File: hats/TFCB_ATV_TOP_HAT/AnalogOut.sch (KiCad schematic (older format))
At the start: 36 parts

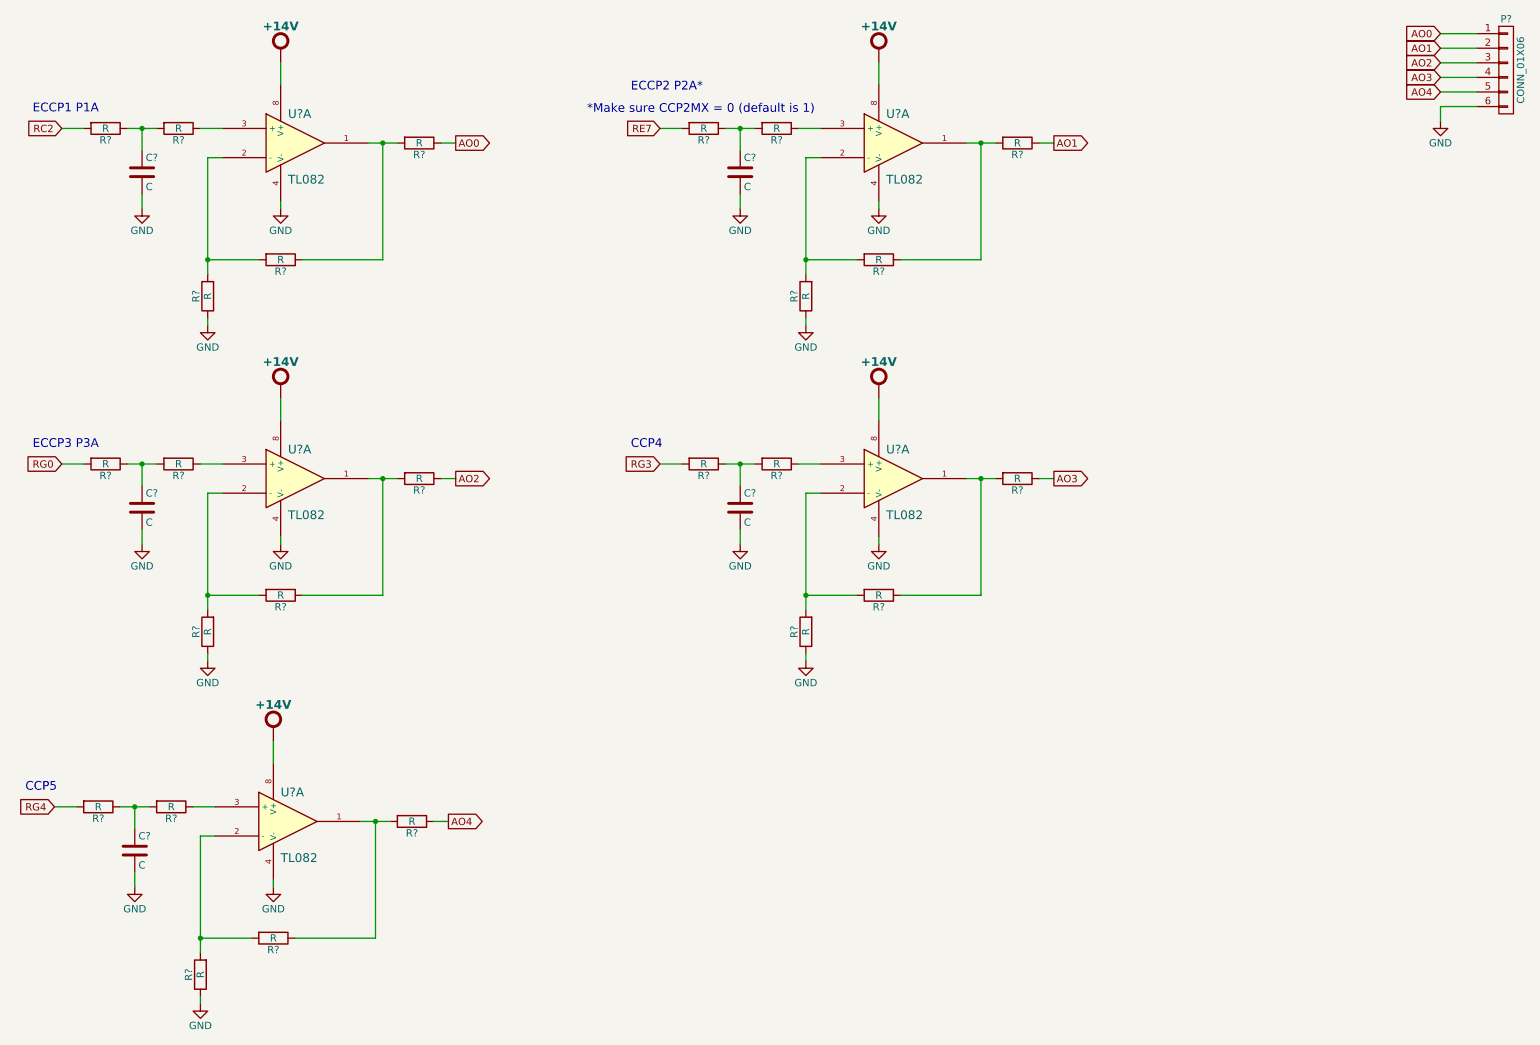
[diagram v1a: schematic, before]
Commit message: Added scanner trigger and current sense cct
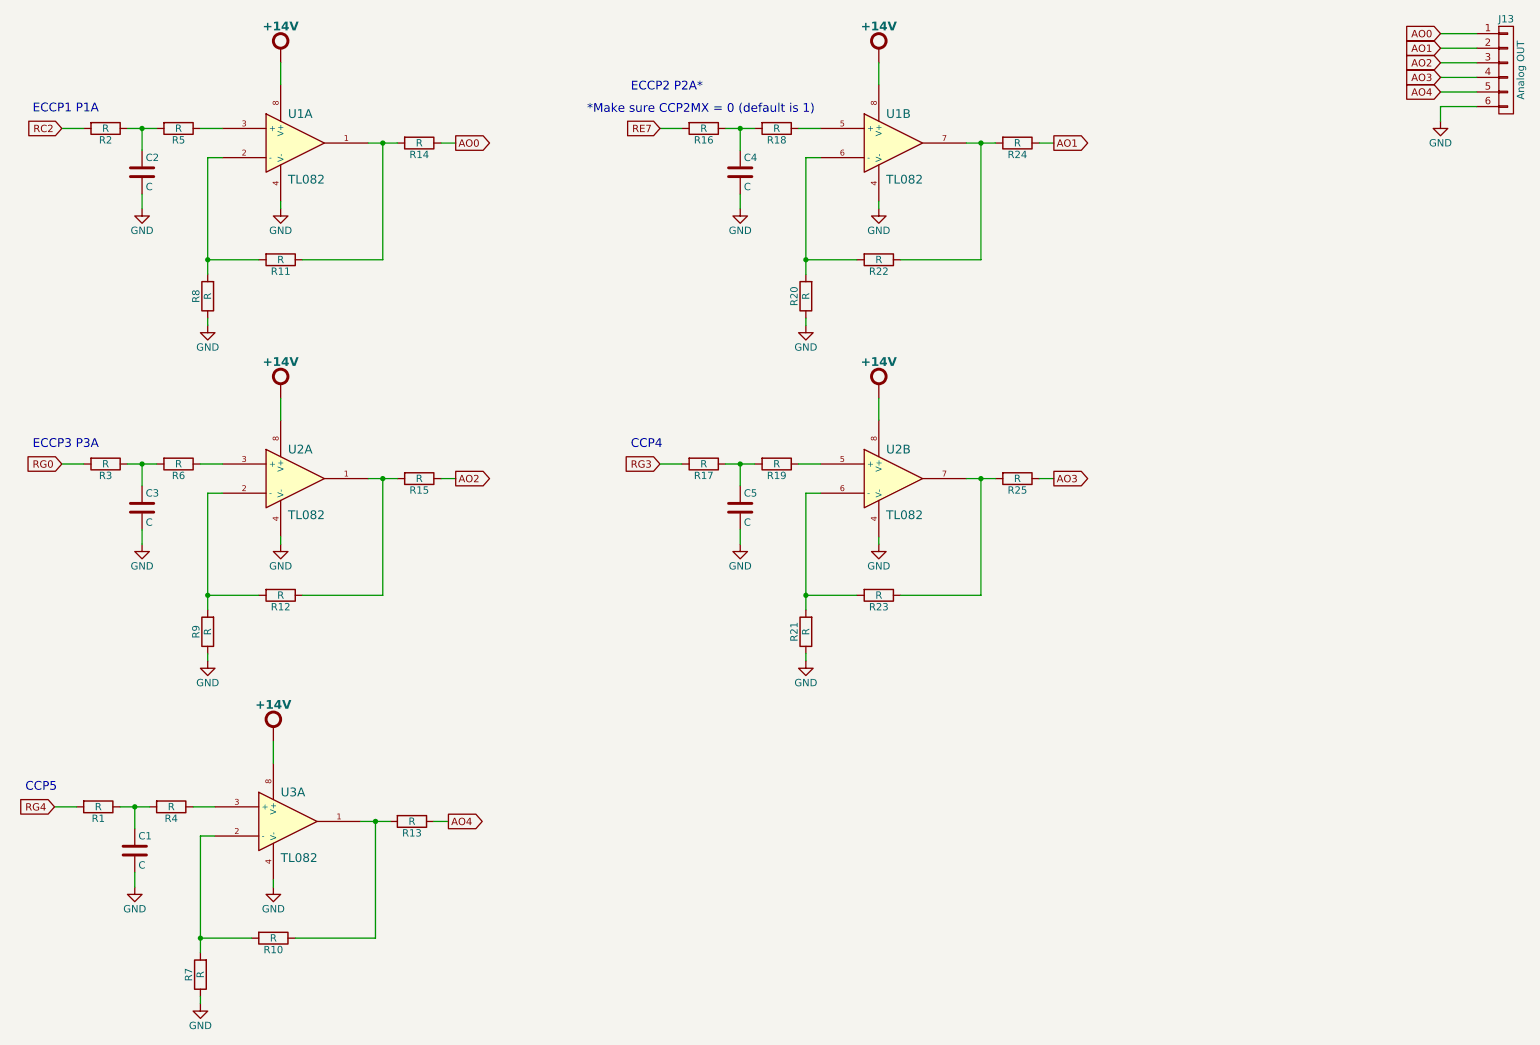
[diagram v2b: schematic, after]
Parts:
- C1, C2, C3, C4, C5: renamed from C?; footprint (none) -> Capacitors_SMD:C_0805_HandSoldering
- J13: renamed from P?; value CONN_01X06 -> Analog OUT; footprint (none) -> bjh-kicad-connector-fp:Weidmuller-SL-5.08-Vertical-6Pole
- R1, R10, R11, R12, R13, R14, R15, R16, R17, R18, R19, R2, R20, R21, R22, R23, R24, R25, R3, R4, R5, R6, R7, R8, R9: renamed from R?; footprint (none) -> Resistors_SMD:R_0805_HandSoldering
- gave numbers to parts that had none: 3
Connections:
- net at R22.1, R24.2: now also U1.7; no longer U1.1
- net at R20.2, R22.2: now also U1.6 (-); no longer U1.2 (-)
- net at R18.1: now also U1.5 (+); no longer U1.3 (+)
- net at R23.1, R25.2: now also U2.7; no longer U2.1
- net at R21.2, R23.2: now also U2.6 (-); no longer U2.2 (-)
- net at R19.1: now also U2.5 (+); no longer U2.3 (+)

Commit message: latest updates
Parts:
- U1, U2, U3: footprint (none) -> Housings_SOIC:SOIC-8_3.9x4.9mm_Pitch1.27mm
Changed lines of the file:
@@
 F 0 "U1" H 2500 1800 60  0000 L CNN
 F 1 "TL082" H 2500 1350 60  0000 L CNN
-F 2 "" H 2550 1600 60  0001 C CNN
+F 2 "Housings_SOIC:SOIC-8_3.9x4.9mm_Pitch1.27mm" H 2550 1600 60  0001 C CNN
 F 3 "" H 2550 1600 60  0000 C CNN
 	1    2550 1600
@@
 F 0 "U2" H 2500 4100 60  0000 L CNN
 F 1 "TL082" H 2500 3650 60  0000 L CNN
-F 2 "" H 2550 3900 60  0001 C CNN
+F 2 "Housings_SOIC:SOIC-8_3.9x4.9mm_Pitch1.27mm" H 2550 3900 60  0001 C CNN
 F 3 "" H 2550 3900 60  0000 C CNN
 	1    2550 3900
@@
 F 0 "U1" H 6600 1800 60  0000 L CNN
 F 1 "TL082" H 6600 1350 60  0000 L CNN
-F 2 "" H 6650 1600 60  0001 C CNN
+F 2 "Housings_SOIC:SOIC-8_3.9x4.9mm_Pitch1.27mm" H 6650 1600 60  0001 C CNN
 F 3 "" H 6650 1600 60  0000 C CNN
 	2    6650 1600
@@
 F 0 "U2" H 6600 4100 60  0000 L CNN
 F 1 "TL082" H 6600 3650 60  0000 L CNN
-F 2 "" H 6650 3900 60  0001 C CNN
+F 2 "Housings_SOIC:SOIC-8_3.9x4.9mm_Pitch1.27mm" H 6650 3900 60  0001 C CNN
 F 3 "" H 6650 3900 60  0000 C CNN
 	2    6650 3900
@@
 F 0 "U3" H 2450 6450 60  0000 L CNN
 F 1 "TL082" H 2450 6000 60  0000 L CNN
-F 2 "" H 2500 6250 60  0001 C CNN
+F 2 "Housings_SOIC:SOIC-8_3.9x4.9mm_Pitch1.27mm" H 2500 6250 60  0001 C CNN
 F 3 "" H 2500 6250 60  0000 C CNN
 	1    2500 6250
